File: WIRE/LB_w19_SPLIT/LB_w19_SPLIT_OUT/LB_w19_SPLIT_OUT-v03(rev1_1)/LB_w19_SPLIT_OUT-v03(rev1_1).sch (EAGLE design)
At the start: 5 parts

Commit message: Updated license text
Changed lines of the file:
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@@
 <instance part="FRAME1" gate="G$1" x="0" y="0"/>
 <instance part="FRAME1" gate="G$2" x="147.32" y="0"/>
-<instance part="U$1" gate="G$1" x="63.5" y="5.08"/>
+<instance part="U$1" gate="G$1" x="33.02" y="10.16"/>
 </instances>
 <busses>

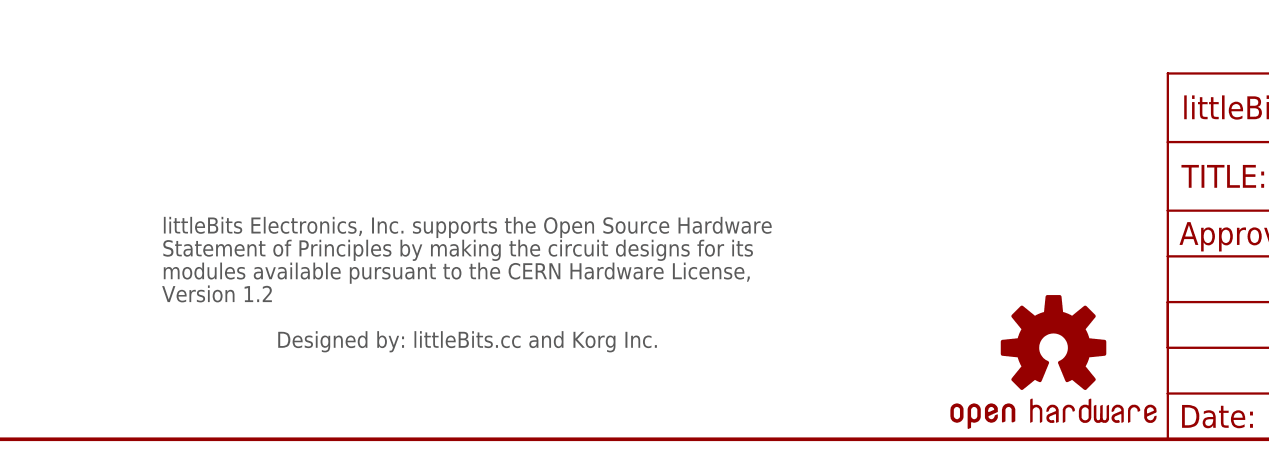
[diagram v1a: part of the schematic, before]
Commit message: Updated license in Korg bits modules
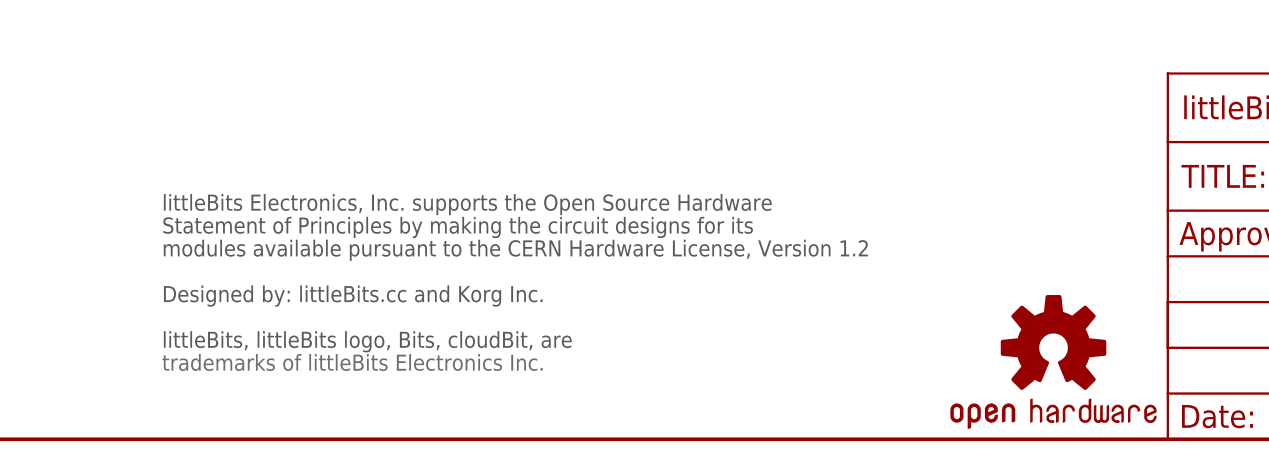
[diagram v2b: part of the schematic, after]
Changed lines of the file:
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@@
 <layer number="111" name="LB_TEXT" color="13" fill="1" visible="yes" active="yes"/>
 <layer number="112" name="tSilk" color="7" fill="1" visible="yes" active="yes"/>
+<layer number="113" name="ReferenceLS" color="7" fill="1" visible="yes" active="yes"/>
 <layer number="116" name="Patch_BOT" color="9" fill="4" visible="yes" active="yes"/>
+<layer number="118" name="Rect_Pads" color="7" fill="1" visible="yes" active="yes"/>
 <layer number="121" name="_tsilk" color="7" fill="1" visible="yes" active="yes"/>
 <layer number="122" name="_bsilk" color="7" fill="1" visible="yes" active="yes"/>
@@
 <instance part="FRAME1" gate="G$1" x="0" y="0"/>
 <instance part="FRAME1" gate="G$2" x="147.32" y="0"/>
-<instance part="U$1" gate="G$1" x="33.02" y="10.16"/>
+<instance part="U$1" gate="G$1" x="33.02" y="12.7"/>
 </instances>
 <busses>
